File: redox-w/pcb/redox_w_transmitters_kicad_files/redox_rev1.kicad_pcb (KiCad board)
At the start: 2 copper layers, 162.2 x 126.5 mm, 104 parts, among them K0 KEYSW, K1 KEYSW, K10 KEYSW, K11 KEYSW, K12 KEYSW, K13 KEYSW, K14 KEYSW, K15 KEYSW, K16 KEYSW, K2 KEYSW, K20 KEYSW, K21 KEYSW, K22 KEYSW, K23 KEYSW, K24 KEYSW, K25 KEYSW, K26 KEYSW, K3 KEYSW, K30 KEYSW, K31 KEYSW, K32 KEYSW, K33 KEYSW, K34 KEYSW, K35 KEYSW, K36 KEYSW, K4 KEYSW, K40 KEYSW, K41 KEYSW, K42 KEYSW, K43 KEYSW, K44 KEYSW, K45 KEYSW, K46 KEYSW, K5 KEYSW, K6 KEYSW

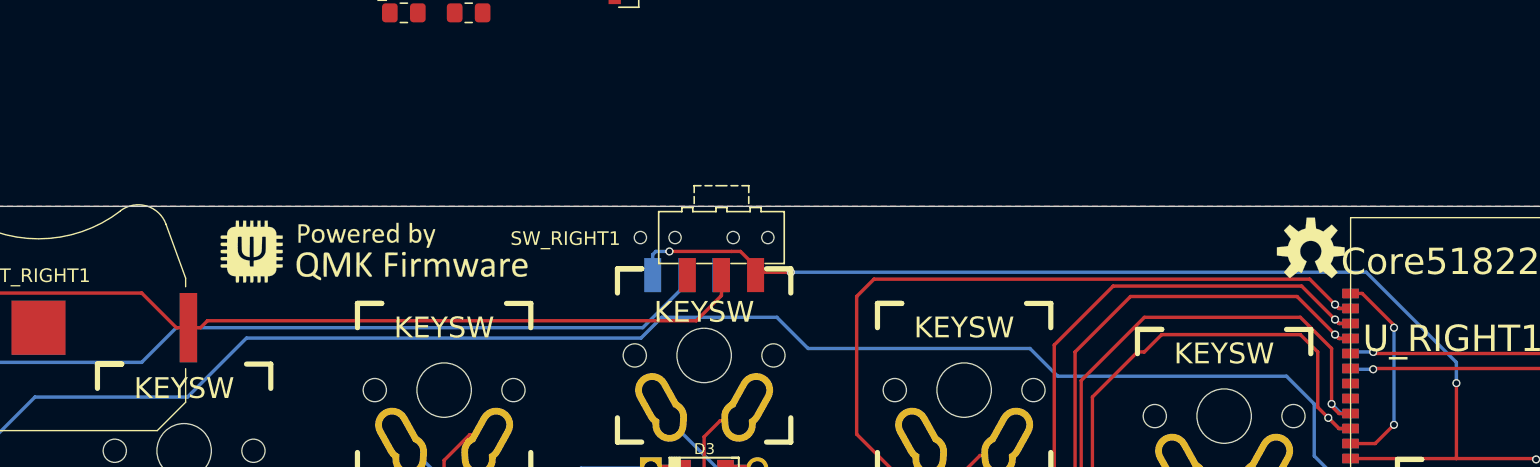
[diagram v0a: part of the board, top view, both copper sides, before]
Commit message: Moved Switch Closer To Battery On PCB
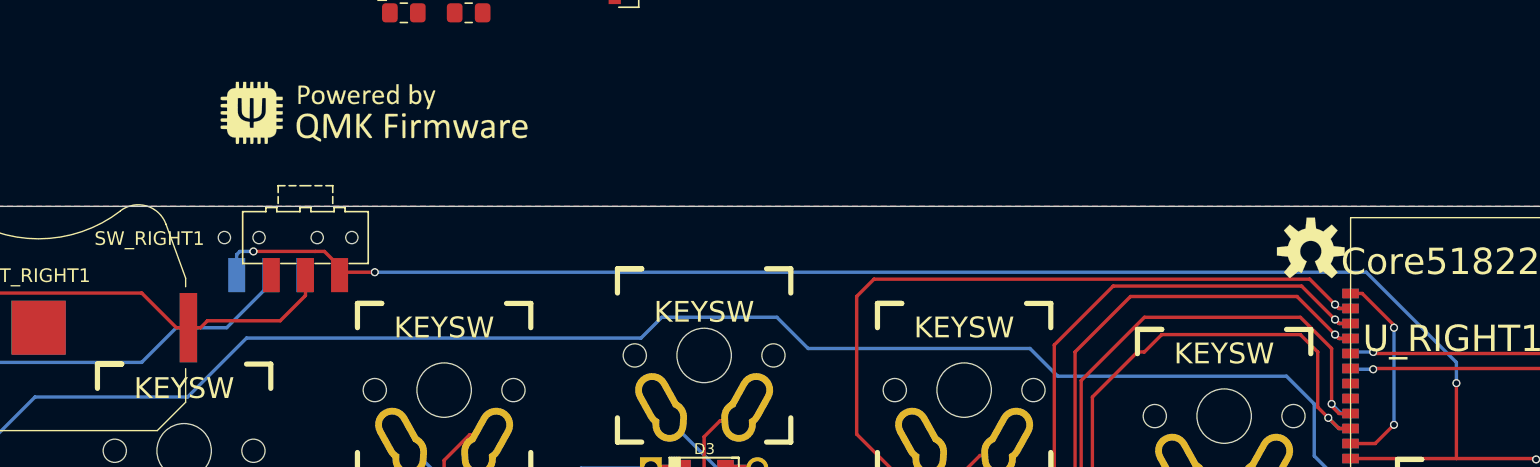
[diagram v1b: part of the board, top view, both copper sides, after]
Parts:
- moved SW_LEFT1 30.5 mm to (119.4, 51.1)
- moved SW_RIGHT1 30.5 mm to (121.9, 51.1)
- moved G*** 10.2 mm to (127.0, 41.9)
- moved G*** 9.91 mm to (127.3, 42.2)
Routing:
- net Net-(BT_LEFT1-Pad1): track 62.5 -> 32.1 mm
- net Net-(BT_RIGHT1-Pad1): track 65.6 -> 35.1 mm
- net VCC: track 148.8 -> 179.3 mm
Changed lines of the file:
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@@
   )
   (module myparts:qmk-badge (layer B.Cu)
-    (at 127 52.07 180)
+    (at 127.254 42.164 180)
     (fp_text reference G*** (at 0 0 180) (layer B.SilkS) hide
       (effects (font (size 1.524 1.524) (thickness 0.3)) (justify mirror))
@@
   )
   (module Button_Switch_SMD:SW_SPDT_CK-JS102011SAQN (layer B.Cu)
-    (at 149.86 51.054)
+    (at 119.38 51.054)
     (descr http://www.ckswitches.com/media/1422/js.pdf)
     (tags "switch spdt")
@@
   )
   (module Button_Switch_SMD:SW_SPDT_CK-JS102011SAQN (layer F.Cu)
-    (at 152.4 51.054 180)
+    (at 121.92 51.054 180)
     (descr http://www.ckswitches.com/media/1422/js.pdf)
     (tags "switch spdt")
@@
   )
   (module myparts:qmk-badge (layer F.Cu)
-    (at 127 52.07)
+    (at 127 41.91)
     (fp_text reference G*** (at 0 0) (layer F.SilkS) hide
       (effects (font (size 1.524 1.524) (thickness 0.3)))
@@
   (segment (start 206.248 67.2465) (end 212.0265 67.2465) (width 0.25) (layer F.Cu) (net 48))
   (segment (start 198.49592 67.2465) (end 206.248 67.2465) (width 0.25) (layer F.Cu) (net 48))
-  (segment (start 206.248 61.722) (end 206.248 60.198) (width 0.25) (layer B.Cu) (net 48))
-  (via (at 157.48 53.594) (size 0.6) (drill 0.4) (layers F.Cu B.Cu) (net 48))
-  (segment (start 206.248 60.198) (end 199.644 53.594) (width 0.25) (layer B.Cu) (net 48))
-  (segment (start 199.644 53.594) (end 157.48 53.594) (width 0.25) (layer B.Cu) (net 48))
-  (segment (start 155.11 53.594) (end 154.9 53.804) (width 0.25) (layer F.Cu) (net 48))
-  (segment (start 157.48 53.594) (end 155.11 53.594) (width 0.25) (layer F.Cu) (net 48))
-  (via (at 148.59 52.07) (size 0.6) (drill 0.4) (layers F.Cu B.Cu) (net 48))
-  (segment (start 153.126002 52.07) (end 148.59 52.07) (width 0.25) (layer F.Cu) (net 48))
-  (segment (start 153.791 52.07) (end 153.126002 52.07) (width 0.25) (layer F.Cu) (net 48))
-  (segment (start 154.9 53.804) (end 154.9 53.179) (width 0.25) (layer F.Cu) (net 48))
-  (segment (start 154.9 53.179) (end 153.791 52.07) (width 0.25) (layer F.Cu) (net 48))
-  (segment (start 147.36 52.304) (end 147.36 53.804) (width 0.25) (layer B.Cu) (net 48))
-  (segment (start 147.594 52.07) (end 147.36 52.304) (width 0.25) (layer B.Cu) (net 48))
-  (segment (start 148.59 52.07) (end 147.594 52.07) (width 0.25) (layer B.Cu) (net 48))
+  (via (at 127 53.594) (size 0.6) (drill 0.4) (layers F.Cu B.Cu) (net 48))
+  (segment (start 124.63 53.594) (end 124.42 53.804) (width 0.25) (layer F.Cu) (net 48))
+  (segment (start 127 53.594) (end 124.63 53.594) (width 0.25) (layer F.Cu) (net 48))
+  (via (at 118.11 52.07) (size 0.6) (drill 0.4) (layers F.Cu B.Cu) (net 48))
+  (segment (start 122.646002 52.07) (end 118.11 52.07) (width 0.25) (layer F.Cu) (net 48))
+  (segment (start 123.311 52.07) (end 122.646002 52.07) (width 0.25) (layer F.Cu) (net 48))
+  (segment (start 124.42 53.804) (end 124.42 53.179) (width 0.25) (layer F.Cu) (net 48))
+  (segment (start 124.42 53.179) (end 123.311 52.07) (width 0.25) (layer F.Cu) (net 48))
+  (segment (start 116.88 52.304) (end 116.88 53.804) (width 0.25) (layer B.Cu) (net 48))
+  (segment (start 117.114 52.07) (end 116.88 52.304) (width 0.25) (layer B.Cu) (net 48))
+  (segment (start 118.11 52.07) (end 117.114 52.07) (width 0.25) (layer B.Cu) (net 48))
   (segment (start 214.34152 67.2465) (end 215.646 68.55098) (width 0.25) (layer B.Cu) (net 48))
   (segment (start 213.49208 67.2465) (end 214.34152 67.2465) (width 0.25) (layer B.Cu) (net 48))
@@
   (segment (start 214.63 117.856) (end 204.724 117.856) (width 0.25) (layer B.Cu) (net 48))
   (segment (start 215.646 116.84) (end 214.63 117.856) (width 0.25) (layer B.Cu) (net 48))
+  (segment (start 206.248 60.198) (end 206.248 61.722) (width 0.25) (layer B.Cu) (net 48))
+  (segment (start 127 53.594) (end 199.644 53.594) (width 0.25) (layer B.Cu) (net 48))
+  (segment (start 199.644 53.594) (end 206.248 60.198) (width 0.25) (layer B.Cu) (net 48))
   (via (at 201.676 57.658) (size 0.6) (drill 0.4) (layers F.Cu B.Cu) (net 49))
   (segment (start 201.676 57.47912) (end 201.676 57.658) (width 0.25) (layer F.Cu) (net 49))
@@
   (segment (start 109.922 60.198) (end 112.462 57.658) (width 0.25) (layer B.Cu) (net 50))
   (segment (start 94.802 60.198) (end 109.922 60.198) (width 0.25) (layer B.Cu) (net 50))
-  (segment (start 149.86 54.429) (end 149.86 53.804) (width 0.25) (layer B.Cu) (net 50))
-  (segment (start 146.631 57.658) (end 149.86 54.429) (width 0.25) (layer B.Cu) (net 50))
-  (segment (start 113.347 57.658) (end 146.631 57.658) (width 0.25) (layer B.Cu) (net 50))
+  (segment (start 119.38 54.429) (end 119.38 53.804) (width 0.25) (layer B.Cu) (net 50))
+  (segment (start 116.151 57.658) (end 119.38 54.429) (width 0.25) (layer B.Cu) (net 50))
+  (segment (start 113.347 57.658) (end 116.151 57.658) (width 0.25) (layer B.Cu) (net 50))
   (segment (start 92.262 57.658) (end 94.802 55.118) (width 0.25) (layer F.Cu) (net 51))
   (segment (start 91.377 57.658) (end 92.262 57.658) (width 0.25) (layer F.Cu) (net 51))
@@
   (segment (start 109.922 55.118) (end 112.462 57.658) (width 0.25) (layer F.Cu) (net 51))
   (segment (start 94.802 55.118) (end 109.922 55.118) (width 0.25) (layer F.Cu) (net 51))
-  (segment (start 152.4 55.304) (end 150.554 57.15) (width 0.25) (layer F.Cu) (net 51))
-  (segment (start 152.4 53.804) (end 152.4 55.304) (width 0.25) (layer F.Cu) (net 51))
+  (segment (start 121.92 53.804) (end 121.92 55.304) (width 0.25) (layer F.Cu) (net 51))
   (segment (start 114.232 57.658) (end 113.347 57.658) (width 0.25) (layer F.Cu) (net 51))
   (segment (start 114.74 57.15) (end 114.232 57.658) (width 0.25) (layer F.Cu) (net 51))
-  (segment (start 150.554 57.15) (end 114.74 57.15) (width 0.25) (layer F.Cu) (net 51))
+  (segment (start 121.92 55.304) (end 120.074 57.15) (width 0.25) (layer F.Cu) (net 51))
+  (segment (start 114.74 57.15) (end 120.074 57.15) (width 0.25) (layer F.Cu) (net 51))
   (via (at 200.152 59.436) (size 0.6) (drill 0.4) (layers F.Cu B.Cu) (net 85))
   (segment (start 213.49208 59.54776) (end 200.26376 59.54776) (width 0.25) (layer F.Cu) (net 85))

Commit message: Arduino ProMicro In Place On PCB, Finished Re-Routing Around It
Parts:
- moved U_RIGHT2 59.4 mm to (151.4, 67.3), turned to 270 degrees
- moved G*** 36.2 mm to (66.0, 102.1)
- moved G*** 35.7 mm to (66.5, 102.1)
- moved ? 8.38 mm to (195.6, 43.7) (x2)
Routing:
- net row0: track 181.0 -> 183.2 mm
- net VCC: track 179.3 -> 181.2 mm

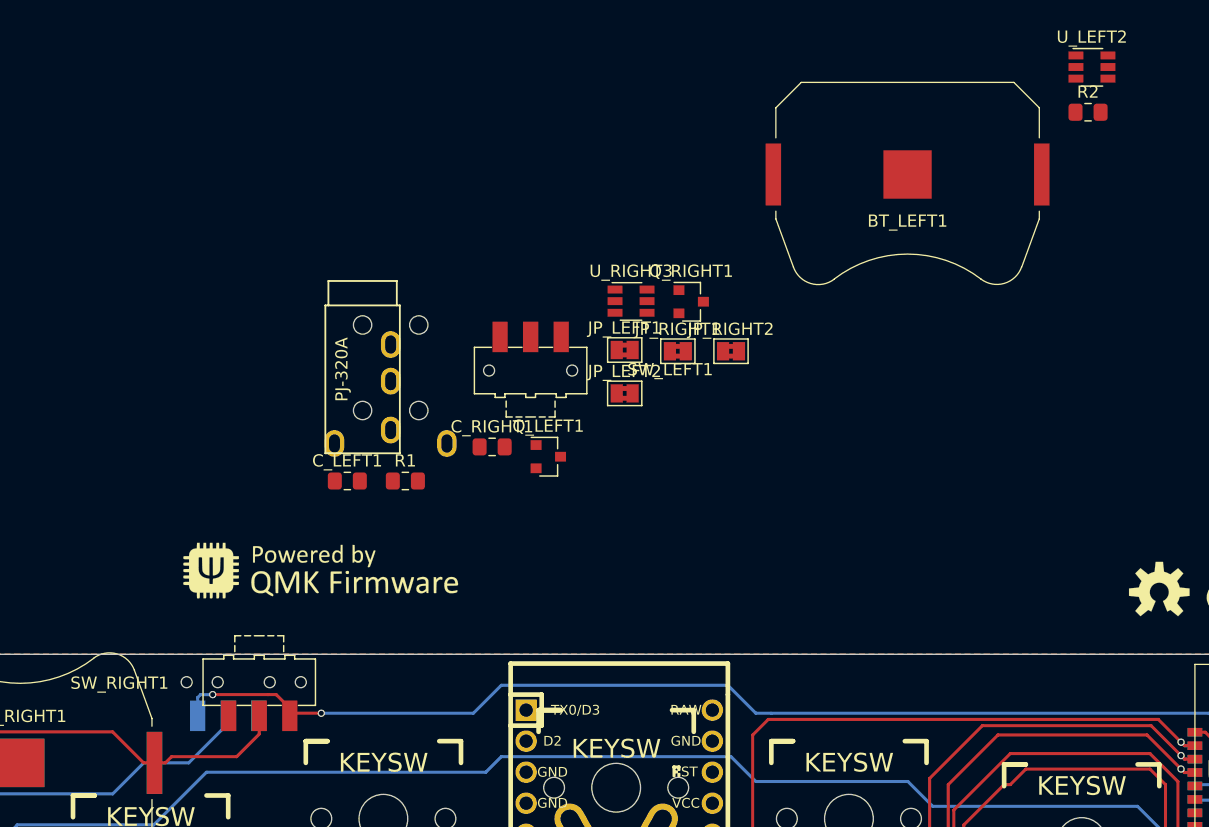
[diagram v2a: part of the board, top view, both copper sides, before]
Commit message: Finished Placing Power Circuitry On PCB
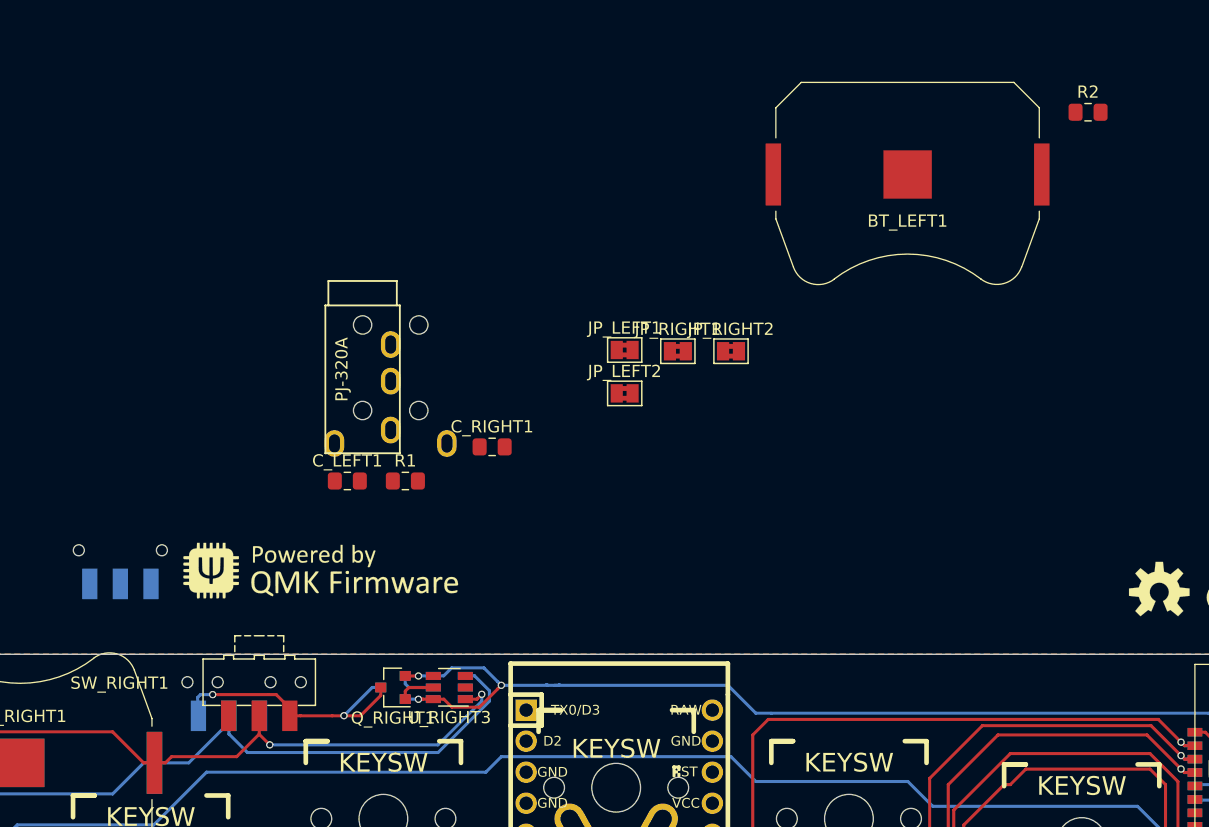
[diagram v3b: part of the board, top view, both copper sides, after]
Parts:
- BT_LEFT1: value Battery_Cel -> Battery_Cell
- Q_LEFT1, SW_LEFT1, U_LEFT2: moved to B.Cu
- moved U_LEFT2 73.1 mm to (137.5, 51.5), turned to 180 degrees
- moved Q_RIGHT1 39.9 mm to (132.9, 51.5), turned to 180 degrees
- moved SW_LEFT1 35.5 mm to (119.4, 51.1)
- moved U_RIGHT3 34.9 mm to (137.5, 51.5), turned to 180 degrees
- moved Q_LEFT1 22.8 mm to (132.9, 51.5), turned to 180 degrees
- moved SW_LEFT1 13.9 mm to (110.6, 40.3)
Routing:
- net Net-(BT_LEFT1-Pad1): track 32.1 -> 60.6 mm
- net Net-(BT_RIGHT1-Pad1): track 35.1 -> 57.3 mm, vias 0 -> 2
- net Net-(Q_RIGHT1-Pad3): track 0.00 -> 19.0 mm, vias 0 -> 2
- net VCC: track 181.2 -> 170.8 mm, vias 4 -> 5
- net Net-(Q_LEFT1-Pad3): track 0.00 -> 3.97 mm
- net Net-(Q_RIGHT1-Pad1): track 0.00 -> 3.07 mm
- net Net-(Q_LEFT1-Pad1): track 0.00 -> 3.06 mm

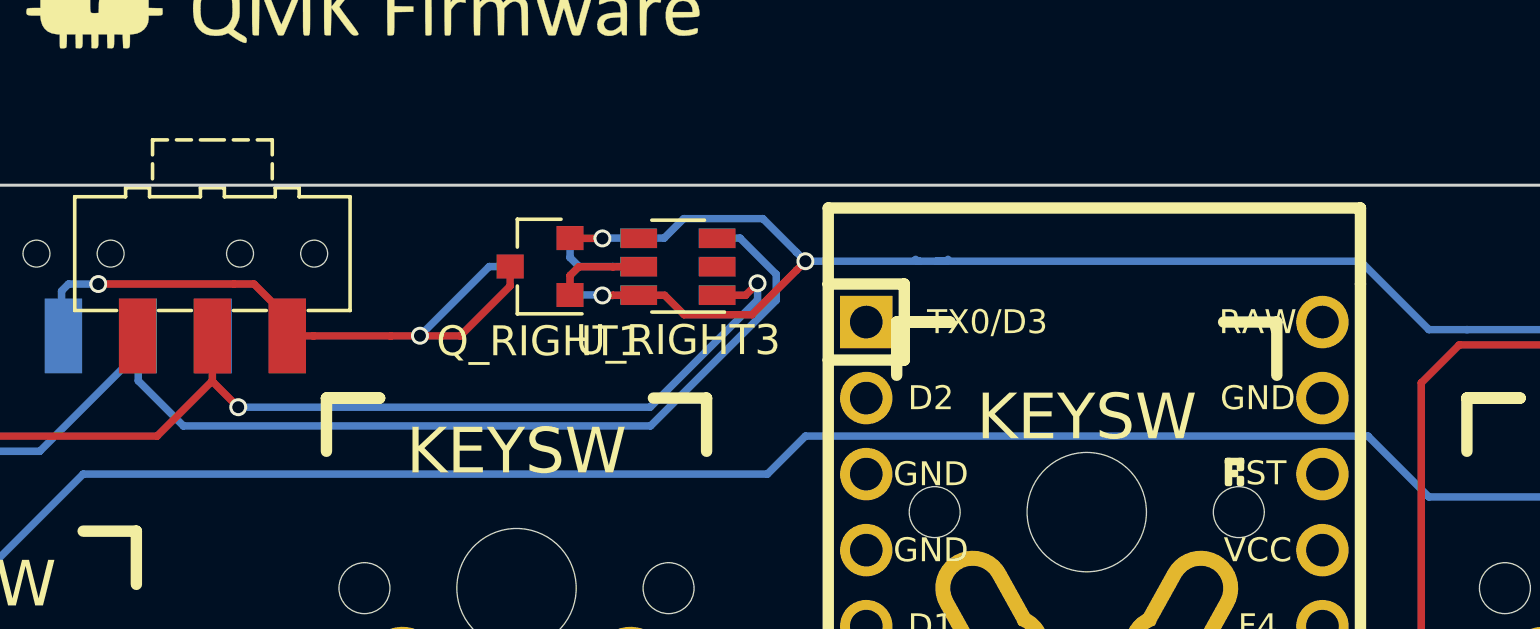
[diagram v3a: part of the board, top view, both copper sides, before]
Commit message: Moved Power Circuitry To Make Room For Serial Lines From YJ To ProMicro
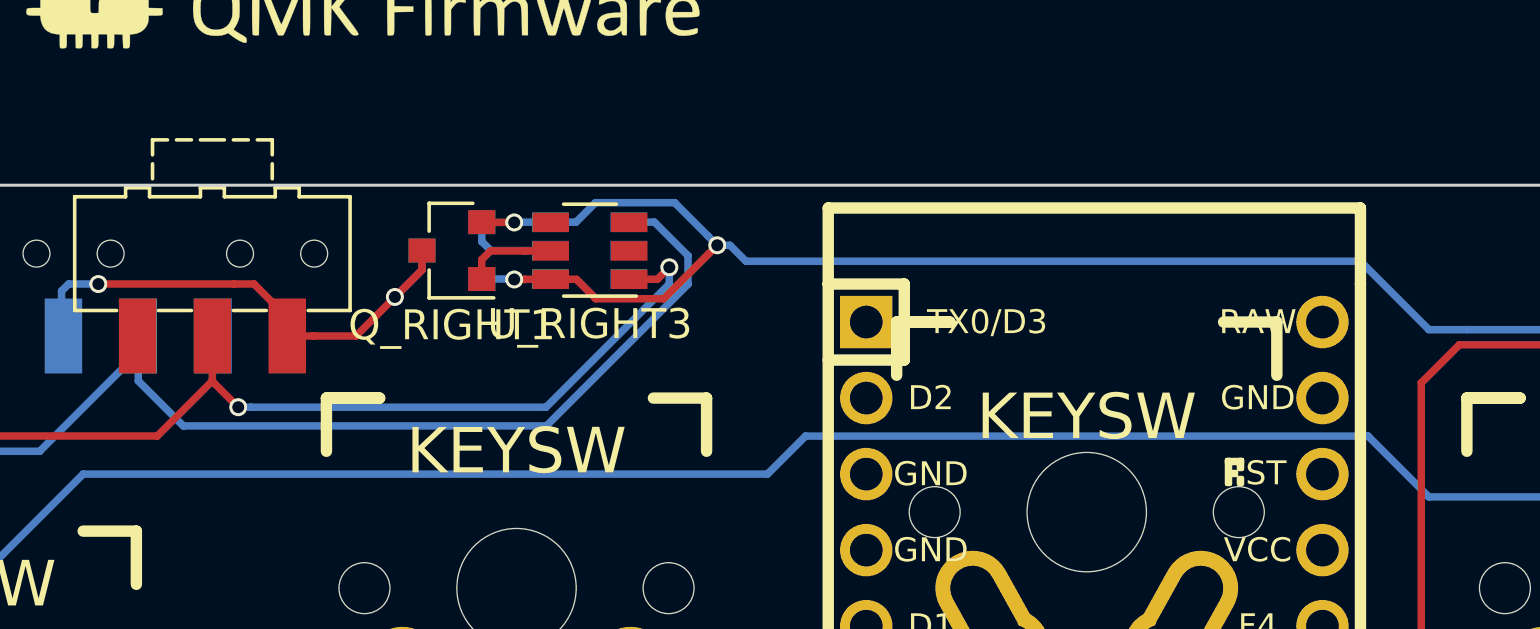
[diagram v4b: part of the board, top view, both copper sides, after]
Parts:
- moved Q_LEFT1 2.99 mm to (129.9, 51.0)
- moved Q_RIGHT1 2.99 mm to (129.9, 51.0)
- moved U_RIGHT3 2.99 mm to (134.5, 51.0)
- moved U_LEFT2 2.99 mm to (134.5, 51.0)
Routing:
- net Net-(BT_RIGHT1-Pad1): track 57.3 -> 54.5 mm
- net Net-(Q_RIGHT1-Pad3): track 19.0 -> 16.3 mm
- net Net-(BT_LEFT1-Pad1): track 60.6 -> 57.9 mm
- net VCC: track 170.8 -> 173.4 mm
- net Net-(Q_LEFT1-Pad3): track 3.97 -> 1.92 mm
